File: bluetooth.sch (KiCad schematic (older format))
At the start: 8 parts

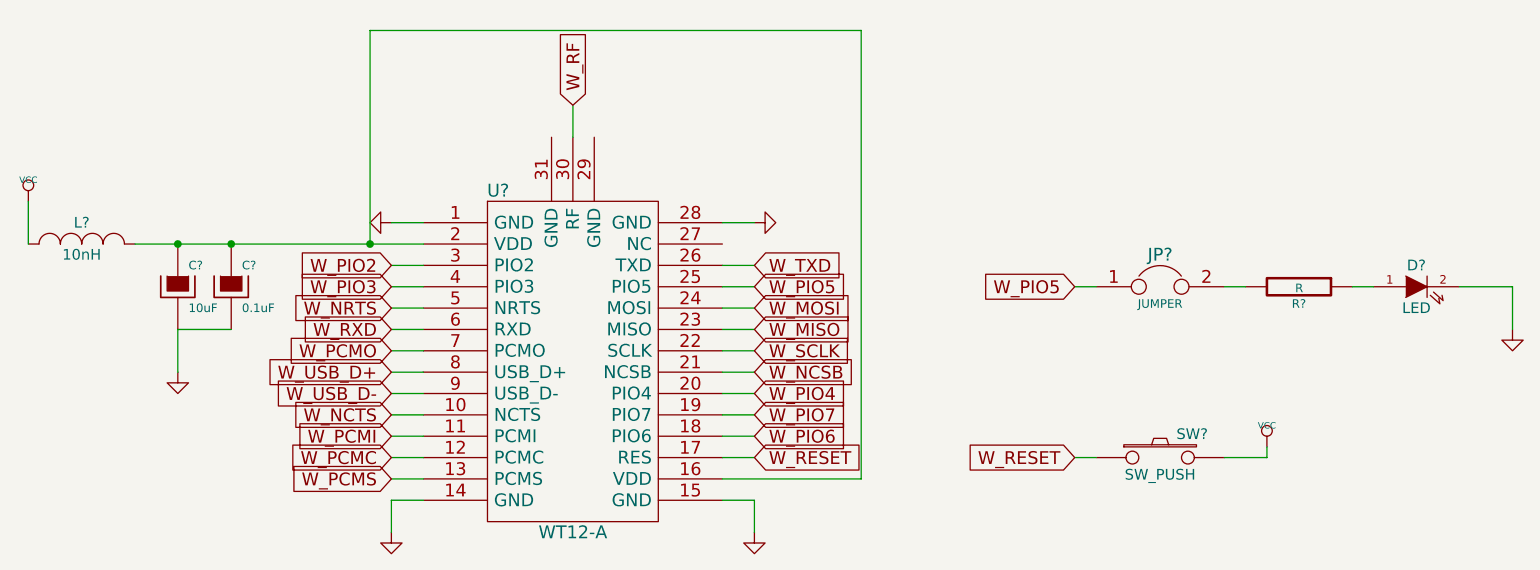
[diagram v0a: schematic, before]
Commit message: Add annotations to parts
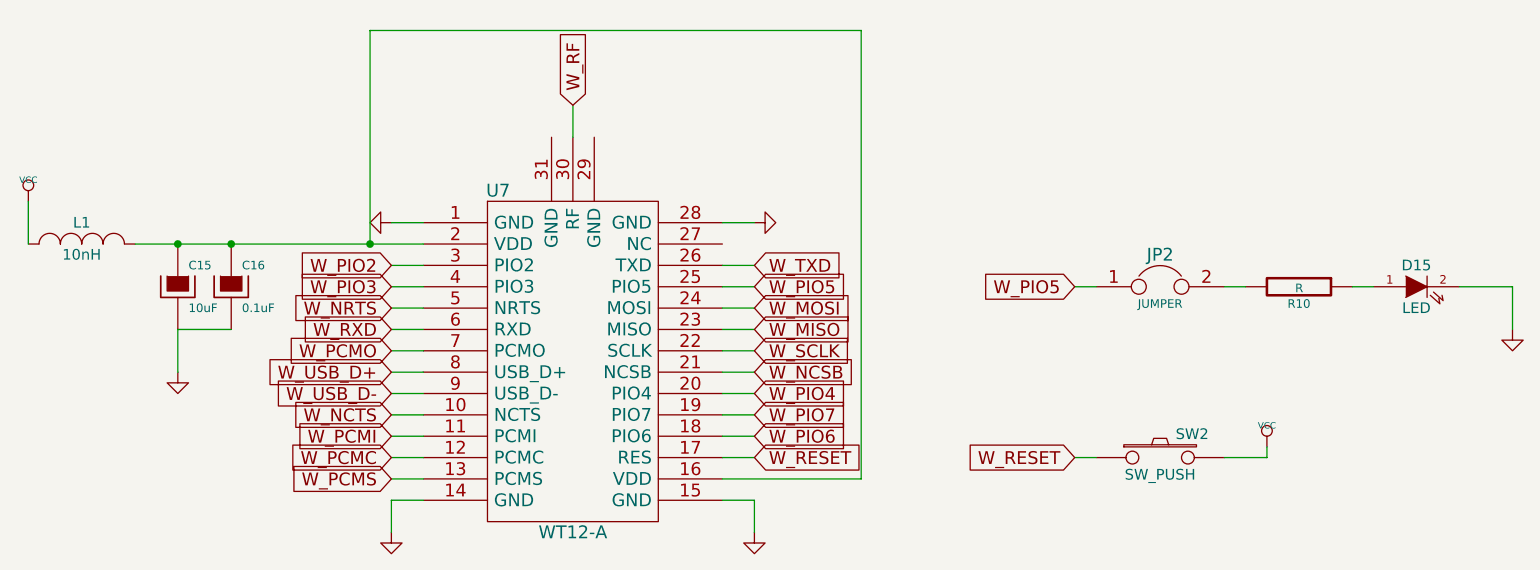
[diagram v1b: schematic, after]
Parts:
- gave numbers to parts that had none: 8
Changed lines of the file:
@@
 $EndDescr
 $Comp
-L WT12-A U?
+L WT12-A U7
 U 1 1 54E5E191
 P 5900 3950
-F 0 "U?" H 5550 4650 60  0000 C CNN
+F 0 "U7" H 5550 4650 60  0000 C CNN
 F 1 "WT12-A" H 5900 3050 60  0000 C CNN
 F 2 "" H 5900 4150 60  0000 C CNN
@@
 W_RF
 $Comp
-L GND #PWR?
+L GND #PWR51
 U 1 1 54E5E1AE
 P 5050 4850
-F 0 "#PWR?" H 5050 4850 30  0001 C CNN
+F 0 "#PWR51" H 5050 4850 30  0001 C CNN
 F 1 "GND" H 5050 4780 30  0001 C CNN
 F 2 "" H 5050 4850 60  0000 C CNN
@@
 $EndComp
 $Comp
-L GND #PWR?
+L GND #PWR50
 U 1 1 54E5E1B4
 P 5050 3400
-F 0 "#PWR?" H 5050 3400 30  0001 C CNN
+F 0 "#PWR50" H 5050 3400 30  0001 C CNN
 F 1 "GND" H 5050 3330 30  0001 C CNN
 F 2 "" H 5050 3400 60  0000 C CNN
@@
 $EndComp
 $Comp
-L GND #PWR?
+L GND #PWR52
 U 1 1 54E5E1BA
 P 6750 3400
-F 0 "#PWR?" H 6750 3400 30  0001 C CNN
+F 0 "#PWR52" H 6750 3400 30  0001 C CNN
 F 1 "GND" H 6750 3330 30  0001 C CNN
 F 2 "" H 6750 3400 60  0000 C CNN
@@
 $EndComp
 $Comp
-L GND #PWR?
+L GND #PWR53
 U 1 1 54E5E1C0
 P 6750 4850
-F 0 "#PWR?" H 6750 4850 30  0001 C CNN
+F 0 "#PWR53" H 6750 4850 30  0001 C CNN
 F 1 "GND" H 6750 4780 30  0001 C CNN
 F 2 "" H 6750 4850 60  0000 C CNN
@@
 $EndComp
 $Comp
-L CP C?
+L CP C15
 U 1 1 54E5E1C6
 P 4050 3700
-F 0 "C?" H 4100 3800 40  0000 L CNN
+F 0 "C15" H 4100 3800 40  0000 L CNN
 F 1 "10uF" H 4100 3600 40  0000 L CNN
 F 2 "" H 4150 3550 30  0000 C CNN
@@
 $EndComp
 $Comp
-L CP C?
+L CP C16
 U 1 1 54E5E1CD
 P 4300 3700
-F 0 "C?" H 4350 3800 40  0000 L CNN
+F 0 "C16" H 4350 3800 40  0000 L CNN
 F 1 "0.1uF" H 4350 3600 40  0000 L CNN
 F 2 "" H 4400 3550 30  0000 C CNN
@@
 $EndComp
 $Comp
-L GND #PWR?
+L GND #PWR49
 U 1 1 54E5E1D4
 P 4050 4100
-F 0 "#PWR?" H 4050 4100 30  0001 C CNN
+F 0 "#PWR49" H 4050 4100 30  0001 C CNN
 F 1 "GND" H 4050 4030 30  0001 C CNN
 F 2 "" H 4050 4100 60  0000 C CNN
@@
 $EndComp
 $Comp
-L INDUCTOR_SMALL L?
+L INDUCTOR_SMALL L1
 U 1 1 54E5E1DA
 P 3600 3500
-F 0 "L?" H 3600 3600 50  0000 C CNN
+F 0 "L1" H 3600 3600 50  0000 C CNN
 F 1 "10nH" H 3600 3450 50  0000 C CNN
 F 2 "" H 3600 3500 60  0000 C CNN
@@
 $EndComp
 $Comp
-L VCC #PWR?
+L VCC #PWR48
 U 1 1 54E5E1E1
 P 3350 3300
-F 0 "#PWR?" H 3350 3400 30  0001 C CNN
+F 0 "#PWR48" H 3350 3400 30  0001 C CNN
 F 1 "VCC" H 3350 3400 30  0000 C CNN
 F 2 "" H 3350 3300 60  0000 C CNN
@@
 Connection ~ 4950 3500
 $Comp
-L SW_PUSH SW?
+L SW_PUSH SW2
 U 1 1 54E72241
 P 8650 4500
-F 0 "SW?" H 8800 4610 50  0000 C CNN
+F 0 "SW2" H 8800 4610 50  0000 C CNN
 F 1 "SW_PUSH" H 8650 4420 50  0000 C CNN
 F 2 "" H 8650 4500 60  0000 C CNN
@@
 W_RESET
 $Comp
-L VCC #PWR?
+L VCC #PWR54
 U 1 1 54E7230E
 P 9150 4450
-F 0 "#PWR?" H 9150 4550 30  0001 C CNN
+F 0 "#PWR54" H 9150 4550 30  0001 C CNN
 F 1 "VCC" H 9150 4550 30  0000 C CNN
 F 2 "" H 9150 4450 60  0000 C CNN
@@
 W_PIO5
 $Comp
-L JUMPER JP?
+L JUMPER JP2
 U 1 1 54E9AF59
 P 8650 3700
-F 0 "JP?" H 8650 3850 60  0000 C CNN
+F 0 "JP2" H 8650 3850 60  0000 C CNN
 F 1 "JUMPER" H 8650 3620 40  0000 C CNN
 F 2 "" H 8650 3700 60  0000 C CNN
@@
 $EndComp
 $Comp
-L R R?
+L R R10
 U 1 1 54E9AF94
 P 9300 3700
-F 0 "R?" V 9380 3700 40  0000 C CNN
+F 0 "R10" V 9380 3700 40  0000 C CNN
 F 1 "R" V 9307 3701 40  0000 C CNN
 F 2 "" V 9230 3700 30  0000 C CNN
@@
 $EndComp
 $Comp
-L LED D?
+L LED D15
 U 1 1 54E9AFFB
 P 9850 3700
-F 0 "D?" H 9850 3800 50  0000 C CNN
+F 0 "D15" H 9850 3800 50  0000 C CNN
 F 1 "LED" H 9850 3600 50  0000 C CNN
 F 2 "" H 9850 3700 60  0000 C CNN
@@
 $EndComp
 $Comp
-L GND #PWR?
+L GND #PWR55
 U 1 1 54E9B03C
 P 10300 3900
-F 0 "#PWR?" H 10300 3900 30  0001 C CNN
+F 0 "#PWR55" H 10300 3900 30  0001 C CNN
 F 1 "GND" H 10300 3830 30  0001 C CNN
 F 2 "" H 10300 3900 60  0000 C CNN

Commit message: WT12 breakout headers are now in place
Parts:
- C15, C16: footprint (none) -> Capacitors_SMD:C_0805_HandSoldering
- JP2: footprint (none) -> replacement_kinesis_controller:JUMPER_2
- R10: footprint (none) -> Resistors_SMD:R_0805_HandSoldering
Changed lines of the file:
@@
 F 0 "U7" H 5550 4650 60  0000 C CNN
 F 1 "WT12-A" H 5900 3050 60  0000 C CNN
-F 2 "" H 5900 4150 60  0000 C CNN
+F 2 "" H 5900 4150 60  0001 C CNN
 F 3 "" H 5900 4150 60  0000 C CNN
 	1    5900 3950
@@
 F 0 "C15" H 4100 3800 40  0000 L CNN
 F 1 "10uF" H 4100 3600 40  0000 L CNN
-F 2 "" H 4150 3550 30  0000 C CNN
+F 2 "Capacitors_SMD:C_0805_HandSoldering" H 4150 3550 30  0001 C CNN
 F 3 "" H 4050 3700 300 0000 C CNN
 	1    4050 3700
@@
 F 0 "C16" H 4350 3800 40  0000 L CNN
 F 1 "0.1uF" H 4350 3600 40  0000 L CNN
-F 2 "" H 4400 3550 30  0000 C CNN
+F 2 "Capacitors_SMD:C_0805_HandSoldering" H 4400 3550 30  0001 C CNN
 F 3 "" H 4300 3700 300 0000 C CNN
 	1    4300 3700
@@
 F 0 "L1" H 3600 3600 50  0000 C CNN
 F 1 "10nH" H 3600 3450 50  0000 C CNN
-F 2 "" H 3600 3500 60  0000 C CNN
+F 2 "" H 3600 3500 60  0001 C CNN
 F 3 "" H 3600 3500 60  0000 C CNN
 	1    3600 3500
@@
 F 0 "SW2" H 8800 4610 50  0000 C CNN
 F 1 "SW_PUSH" H 8650 4420 50  0000 C CNN
-F 2 "" H 8650 4500 60  0000 C CNN
+F 2 "" H 8650 4500 60  0001 C CNN
 F 3 "" H 8650 4500 60  0000 C CNN
 	1    8650 4500
@@
 F 0 "JP2" H 8650 3850 60  0000 C CNN
 F 1 "JUMPER" H 8650 3620 40  0000 C CNN
-F 2 "" H 8650 3700 60  0000 C CNN
+F 2 "replacement_kinesis_controller:JUMPER_2" H 8650 3700 60  0001 C CNN
 F 3 "" H 8650 3700 60  0000 C CNN
 	1    8650 3700
@@
 F 0 "R10" V 9380 3700 40  0000 C CNN
 F 1 "R" V 9307 3701 40  0000 C CNN
-F 2 "" V 9230 3700 30  0000 C CNN
+F 2 "Resistors_SMD:R_0805_HandSoldering" V 9230 3700 30  0001 C CNN
 F 3 "" H 9300 3700 30  0000 C CNN
 	1    9300 3700
@@
 F 0 "D15" H 9850 3800 50  0000 C CNN
 F 1 "LED" H 9850 3600 50  0000 C CNN
-F 2 "" H 9850 3700 60  0000 C CNN
+F 2 "" H 9850 3700 60  0001 C CNN
 F 3 "" H 9850 3700 60  0000 C CNN
 	1    9850 3700

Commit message: Add regular LED footprints
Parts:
- D15: footprint (none) -> LEDs:LED-0805
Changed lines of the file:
@@
 F 0 "D15" H 9850 3800 50  0000 C CNN
 F 1 "LED" H 9850 3600 50  0000 C CNN
-F 2 "" H 9850 3700 60  0001 C CNN
+F 2 "LEDs:LED-0805" H 9850 3700 60  0001 C CNN
 F 3 "" H 9850 3700 60  0000 C CNN
 	1    9850 3700

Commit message: More footprints
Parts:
- L1: footprint (none) -> Resistors_SMD:R_0805_HandSoldering
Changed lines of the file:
@@
 F 0 "L1" H 3600 3600 50  0000 C CNN
 F 1 "10nH" H 3600 3450 50  0000 C CNN
-F 2 "" H 3600 3500 60  0001 C CNN
+F 2 "Resistors_SMD:R_0805_HandSoldering" H 3600 3500 60  0001 C CNN
 F 3 "" H 3600 3500 60  0000 C CNN
 	1    3600 3500

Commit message: Add WT12 footprint
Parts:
- U7: footprint (none) -> replacement_kinesis_controller:WT12
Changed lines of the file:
@@
 F 0 "U7" H 5550 4650 60  0000 C CNN
 F 1 "WT12-A" H 5900 3050 60  0000 C CNN
-F 2 "" H 5900 4150 60  0001 C CNN
+F 2 "replacement_kinesis_controller:WT12" H 5900 4150 60  0001 C CNN
 F 3 "" H 5900 4150 60  0000 C CNN
 	1    5900 3950

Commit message: Basically done footprint assignment now...?
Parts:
- SW2: footprint (none) -> Buttons_Switches_SMD:SW_SPST_PTS645
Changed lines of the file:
@@
 F 0 "SW2" H 8800 4610 50  0000 C CNN
 F 1 "SW_PUSH" H 8650 4420 50  0000 C CNN
-F 2 "" H 8650 4500 60  0001 C CNN
+F 2 "Buttons_Switches_SMD:SW_SPST_PTS645" H 8650 4500 60  0001 C CNN
 F 3 "" H 8650 4500 60  0000 C CNN
 	1    8650 4500

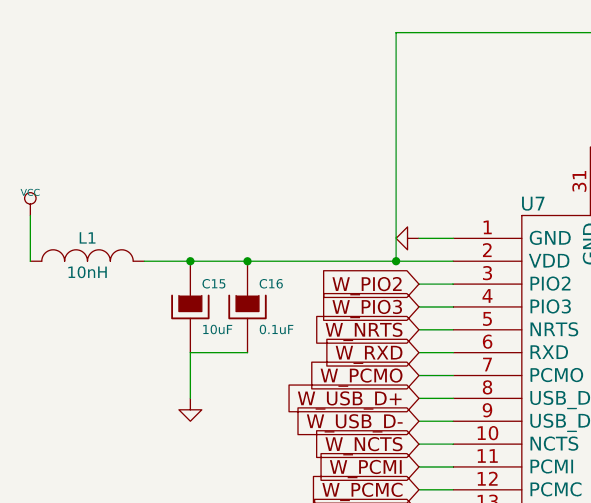
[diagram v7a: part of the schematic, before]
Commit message: Fix bluetooth breakout pin nets and add ground pour to USB boards
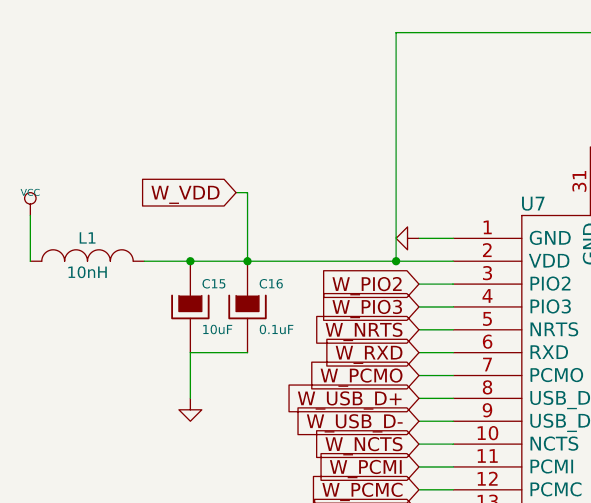
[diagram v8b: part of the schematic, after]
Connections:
- net W_VDD: now reaches C15.1, C16.1, L1.2, U7.16 (VDD), U7.2 (VDD)
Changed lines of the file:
@@
 W_RF
 $Comp
-L GND #PWR048
+L GND #PWR047
 U 1 1 54E5E1AE
 P 5050 4850
-F 0 "#PWR048" H 5050 4850 30  0001 C CNN
+F 0 "#PWR047" H 5050 4850 30  0001 C CNN
 F 1 "GND" H 5050 4780 30  0001 C CNN
 F 2 "" H 5050 4850 60  0000 C CNN
@@
 $EndComp
 $Comp
-L GND #PWR049
+L GND #PWR048
 U 1 1 54E5E1B4
 P 5050 3400
-F 0 "#PWR049" H 5050 3400 30  0001 C CNN
+F 0 "#PWR048" H 5050 3400 30  0001 C CNN
 F 1 "GND" H 5050 3330 30  0001 C CNN
 F 2 "" H 5050 3400 60  0000 C CNN
@@
 $EndComp
 $Comp
-L GND #PWR050
+L GND #PWR049
 U 1 1 54E5E1BA
 P 6750 3400
-F 0 "#PWR050" H 6750 3400 30  0001 C CNN
+F 0 "#PWR049" H 6750 3400 30  0001 C CNN
 F 1 "GND" H 6750 3330 30  0001 C CNN
 F 2 "" H 6750 3400 60  0000 C CNN
@@
 $EndComp
 $Comp
-L GND #PWR051
+L GND #PWR050
 U 1 1 54E5E1C0
 P 6750 4850
-F 0 "#PWR051" H 6750 4850 30  0001 C CNN
+F 0 "#PWR050" H 6750 4850 30  0001 C CNN
 F 1 "GND" H 6750 4780 30  0001 C CNN
 F 2 "" H 6750 4850 60  0000 C CNN
@@
 $EndComp
 $Comp
-L GND #PWR052
+L GND #PWR051
 U 1 1 54E5E1D4
 P 4050 4100
-F 0 "#PWR052" H 4050 4100 30  0001 C CNN
+F 0 "#PWR051" H 4050 4100 30  0001 C CNN
 F 1 "GND" H 4050 4030 30  0001 C CNN
 F 2 "" H 4050 4100 60  0000 C CNN
@@
 $EndComp
 $Comp
-L VCC #PWR053
+L VCC #PWR052
 U 1 1 54E5E1E1
 P 3350 3300
-F 0 "#PWR053" H 3350 3400 30  0001 C CNN
+F 0 "#PWR052" H 3350 3400 30  0001 C CNN
 F 1 "VCC" H 3350 3400 30  0000 C CNN
 F 2 "" H 3350 3300 60  0000 C CNN
@@
 W_RESET
 $Comp
-L VCC #PWR054
+L VCC #PWR053
 U 1 1 54E7230E
 P 9150 4450
-F 0 "#PWR054" H 9150 4550 30  0001 C CNN
+F 0 "#PWR053" H 9150 4550 30  0001 C CNN
 F 1 "VCC" H 9150 4550 30  0000 C CNN
 F 2 "" H 9150 4450 60  0000 C CNN
@@
 $EndComp
 $Comp
-L GND #PWR055
+L GND #PWR054
 U 1 1 54E9B03C
 P 10300 3900
-F 0 "#PWR055" H 10300 3900 30  0001 C CNN
+F 0 "#PWR054" H 10300 3900 30  0001 C CNN
 F 1 "GND" H 10300 3830 30  0001 C CNN
 F 2 "" H 10300 3900 60  0000 C CNN
@@
 Wire Wire Line
 	8350 3700 8250 3700
+Text GLabel 4250 3200 0    60   Input ~ 0
+W_VDD
+Wire Wire Line
+	4250 3200 4300 3200
+Wire Wire Line
+	4300 3200 4300 3500
 $EndSCHEMATC
